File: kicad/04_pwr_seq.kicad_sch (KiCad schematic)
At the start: 3 parts, among them U401 TPS3808G01DBVR

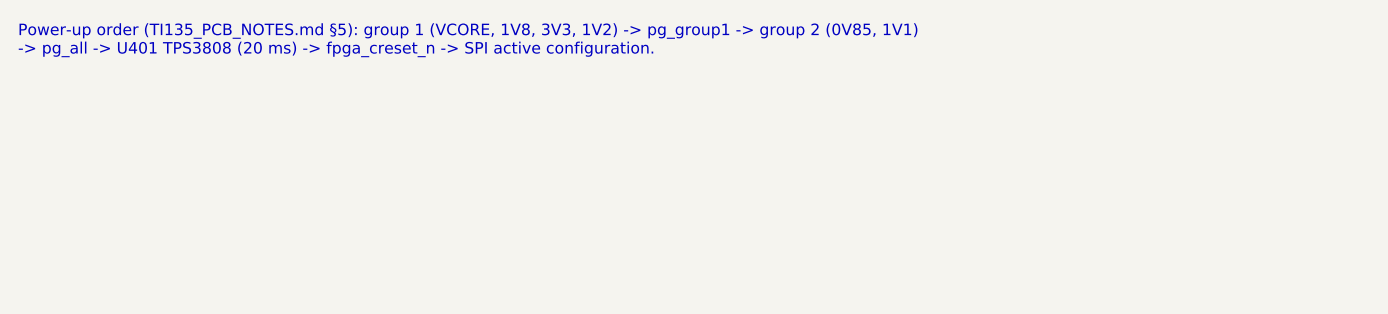
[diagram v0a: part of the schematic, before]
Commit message: Placement with KiCadRoutingTools; Ethernet PHY changed to RTL8211FDI-CG
- Sheet 09 redone for the RTL8211FDI-CG (C692886; the KSZ9031 had 16 orderable, and the
  Agilex 5 card makes the same change). It runs from 3V3 only, with an internal 1.0 V core LDO
  and RGMII pads at 1.8 V from its pad LDO; all nine straps are fitted. PHYRSTB is a 3.3 V
  input, so it is driven through a 74LVC1G07 open drain. The jack LED is driven straight
  from LED2.
- The 1V2 buck (U321) is removed. Power budget and docs updated.
- make_board sets pad pin functions/types, so the placer reads the Y701 oscillator correctly.
- Placement: placement/ holds the inputs (groups, prep, intent fixes, judging chain). Seed 1
  of 12 was chosen by the quick-route judge and applied with tools/apply_placement.py.
  build_pcb.sh no longer rebuilds by default; --rebuild restores the poses.
- tools/jlc: the jlc-tools submodule.

Co-Authored-By: Claude Opus 5.5 <noreply@anthropic.com>
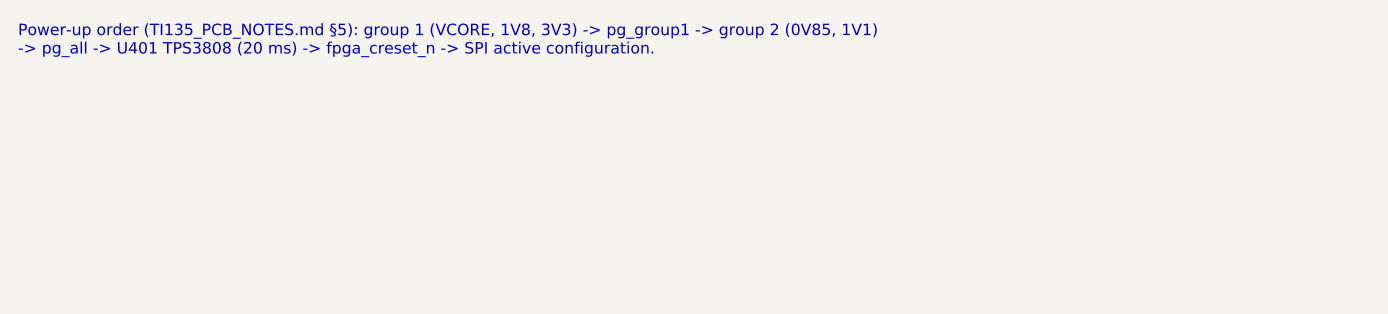
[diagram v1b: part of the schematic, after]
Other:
- note added: "Power-up order (TI135_PCB_NOTES.md §5): group 1 (VCORE, 1V8, 3V3) -> pg_group1 -> group 2 (0V85, 1V1) -> pg_all -> U401 TPS3808 (20 ms) -> fpga_creset_n -> SPI active configuration."
- note removed: "Power-up order (TI135_PCB_NOTES.md §5): group 1 (VCORE, 1V8, 3V3, 1V2) -> pg_group1 -> group 2 (0V85, 1V1) -> pg_all -> U401 TPS3808 (20 ms) -> fpga_creset_n -> SPI active configuration."
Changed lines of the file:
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@@
 		(comment 1 "Efinix Ti135N484I3 control card for the AC lab PSU baseboard")
 	)
-	(text "Power-up order (TI135_PCB_NOTES.md §5): group 1 (VCORE, 1V8, 3V3, 1V2) -> pg_group1 -> group 2 (0V85, 1V1)\n-> pg_all -> U401 TPS3808 (20 ms) -> fpga_creset_n -> SPI active configuration."
+	(text "Power-up order (TI135_PCB_NOTES.md §5): group 1 (VCORE, 1V8, 3V3) -> pg_group1 -> group 2 (0V85, 1V1)\n-> pg_all -> U401 TPS3808 (20 ms) -> fpga_creset_n -> SPI active configuration."
 		(exclude_from_sim no)
 		(at 17.78 17.78 0)

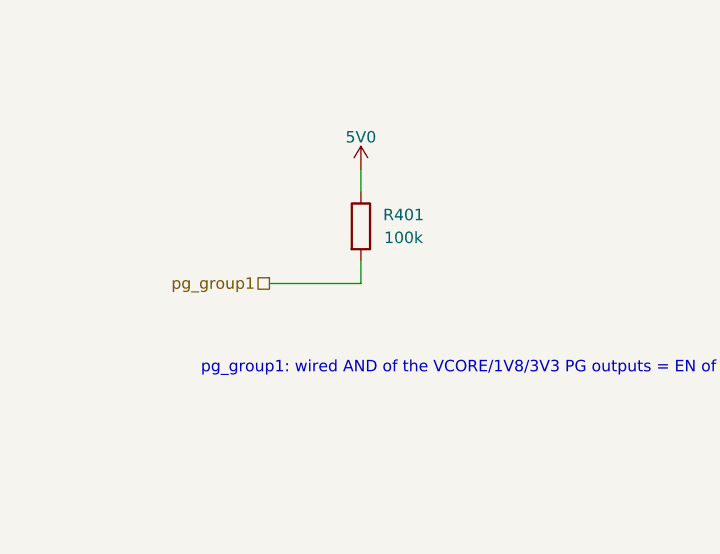
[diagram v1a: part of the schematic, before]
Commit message: LPDDR4 hand routing: Agilex DRAM escape copied, byte lanes routed, DQ swizzle by hand
- U801 decoupling = the Agilex U12 set (sheet 08: 29 x 100n 0201, 22u/1u 0402, LCSC from the
  Agilex card), placed at the Agilex positions on the same via pairs; R802 (ZQ) at R43's spot;
  CA/CKE T-branches on B.Cu copied (tools/ddr/copy_dram_escape.py)
- LPDDR4 vias not on a BGA ball removed (T-branch centre vias kept)
- Schematic: #PWR/#FLG references made unique per sheet (prefix = sheet number); the
  duplicates blocked Update PCB from Schematic
- DQ swizzle now edited by hand in the schematic (bytes 0 and 2); efinity/pinplan/lpddr4_swizzle.json
  is not updated yet
- Byte lanes routed by hand (work in progress)

Known open (WIP): byte 2 - ddr_dq22 on two U501 balls (AA16, W16), ddr_dq21 has no U501 ball;
DRC shows 2 shorts at U501 Y16/W16 (dq21/dq17 tracks).

Co-Authored-By: Claude Opus 5.5 <noreply@anthropic.com>
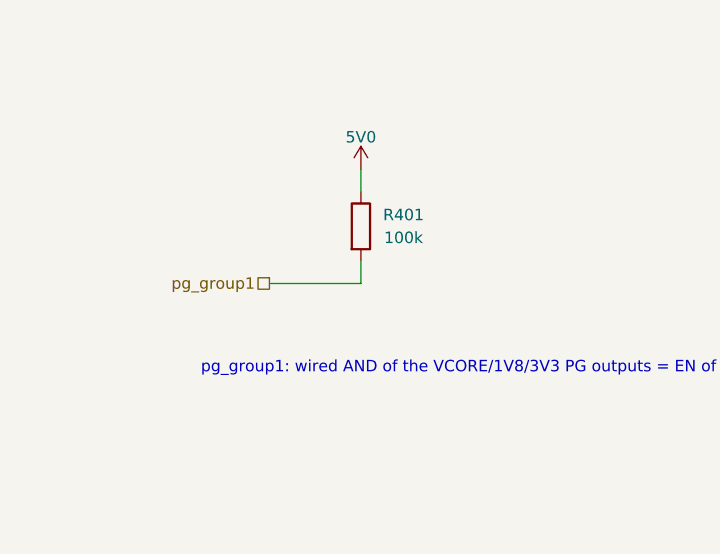
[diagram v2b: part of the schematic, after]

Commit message: LCSC numbers for all JLC parts; Y701 -> YXC OT322525MJBA4SL
- tools/set_lcsc.py: one table (value, footprint) -> LCSC, fills empty LCSC fields in the
  sheets; 312 symbols. JLC basic parts where available, cap voltages checked per rail,
  VCORE divider 0.1 % (no 0.5 % in stock). Board fields synced with add_parts.py.
- Y701: the SiT8924 has no JLC stock; now YXC OT322525MJBA4SL (C669088, 3225), EN tied
  to 1V8. R701/C701 moved 0.5 mm to clear its courtyard. Netlist change: Y701 pin 1 -> 1V8.
- Only U501 (Ti135) is left without LCSC (global sourcing / consigned).
- DRC: schematic parity 0.

Co-Authored-By: Claude Opus 5.5 <noreply@anthropic.com>
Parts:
- C401: LCSC (none) -> C1525
- R401: LCSC (none) -> C25741
- U401: LCSC (none) -> C19653
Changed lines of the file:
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@@
+			)
+		)
+		(property "LCSC" "C25741"
+			(at 55.88 57.15 0)
+			(effects
+				(font
+					(size 1.27 1.27)
+				)
+				(hide yes)
 			)
 		)
@@
 			)
 		)
+		(property "LCSC" "C1525"
+			(at 190.5 63.5 0)
+			(effects
+				(font
+					(size 1.27 1.27)
+				)
+				(hide yes)
+			)
+		)
 		(pin "1"
 		)
@@
 			)
 		)
+		(property "LCSC" "C19653"
+			(at 152.4 76.2 0)
+			(effects
+				(font
+					(size 1.27 1.27)
+				)
+				(hide yes)
+			)
+		)
